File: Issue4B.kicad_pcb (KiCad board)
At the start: 2 copper layers, 213.1 x 130 mm, 207 parts, among them IC1 ULA, IC10 4116, IC11 4116, IC12 4116, IC13 4116, IC14 LM1889, IC15 4532, IC16 4532, IC17 4532, IC18 4532, IC19 4532, IC2 Z80, IC20 4532, IC21 4532, IC22 4532, IC23 LS32, IC24 LS00, IC25 LS157, IC26 LS157, IC3 LS157, IC4 LS157, IC5 ROM, IC6 4116, IC7 4116, IC8 4116, IC9 4116, J7 Barrel_Jack_MountingPin, SW1 SW_SPDT, T1 Transformer_1P_1S, X1 14Mhz, X2 4.43Mhz

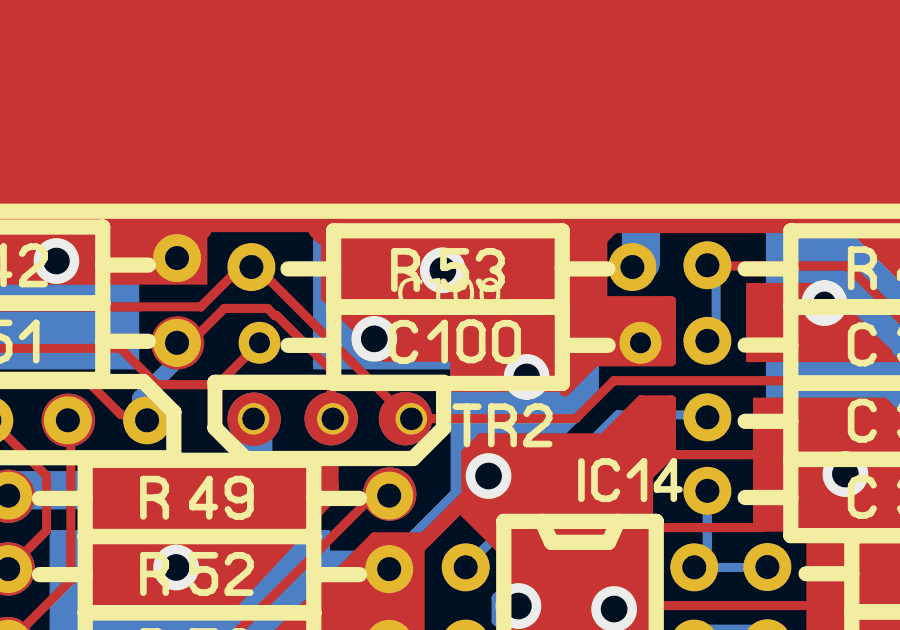
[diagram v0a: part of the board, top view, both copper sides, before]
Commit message: Correct values for C100 and C101
Update values and layout for C100 and C101. Taken from Issue 6A schematic.
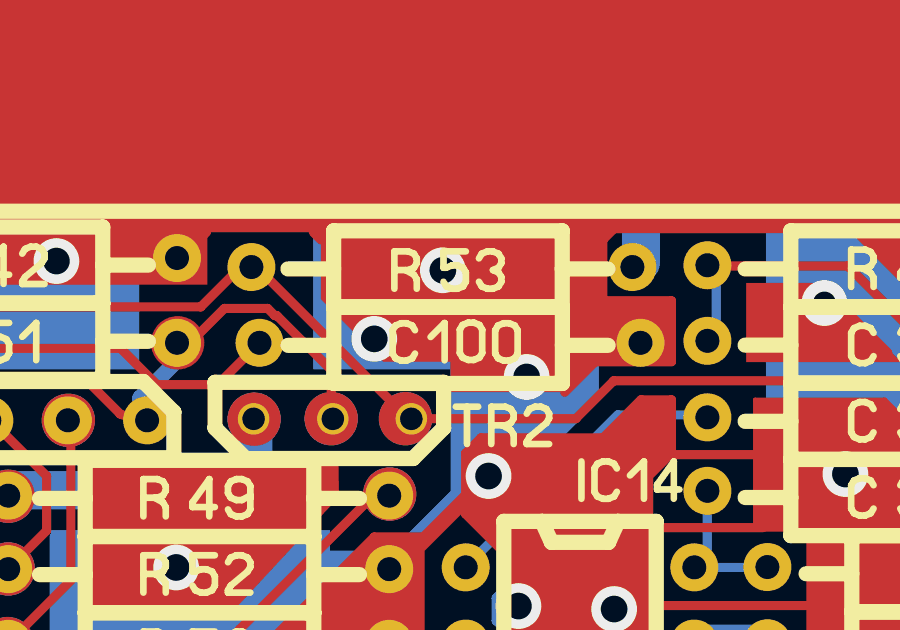
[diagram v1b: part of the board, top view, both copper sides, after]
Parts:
- C100: value 390R -> 10nF; footprint Mod:R_Yageo_L3.6mm_D1.6mm_P12.70mm_Horizontal -> Mod:C_Axial_L3.8mm_D2.6mm_P12.70mm_Horizontal
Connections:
- C101 pad 2: GND -> +V_IN
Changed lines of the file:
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@@
 		)
 	)
-	(footprint "Mod:R_Yageo_L3.6mm_D1.6mm_P12.70mm_Horizontal"
+	(footprint "Mod:C_Axial_L3.8mm_D2.6mm_P12.70mm_Horizontal"
 		(locked yes)
 		(layer "F.Cu")
 		(at 62.7695 63.526)
-		(descr "Resistor, Yageo series, Axial, Horizontal, pin pitch=12.7mm, 0.167W, length*diameter=3.6*1.6mm^2, http://cdn-reichelt.de/documents/datenblatt/B400/1_4W%23YAG.pdf")
-		(tags "Resistor Yageo series Axial Horizontal pin pitch 12.7mm 0.167W length 3.6mm diameter 1.6mm")
+		(descr "C, Axial series, Axial, Horizontal, pin pitch=12.7mm, length*diameter=3.8*2.6mm^2, http://www.vishay.com/docs/45231/arseries.pdf")
+		(tags "C Axial series Axial Horizontal pin pitch 12.7mm  length 3.8mm diameter 2.6mm")
 		(property "Reference" "C100"
-			(at 6.33 -1.62 0)
+			(at 6.35 0.127 0)
 			(layer "F.SilkS")
+			(hide yes)
 			(effects
 				(font
@@
 			)
 		)
-		(property "Value" "390R"
-			(at 6.35 -0.01 0)
+		(property "Value" "10nF"
+			(at 6.35 2.42 0)
 			(layer "F.Fab")
 			(effects
@@
 			)
 		)
-		(property "Description" ""
+		(property "Description" "Unpolarized capacitor, small symbol"
 			(at 0 0 0)
 			(layer "F.Fab")
@@
 			)
 		)
-		(property ki_fp_filters "R_*")
+		(property ki_fp_filters "C_*")
 		(sheetname "/")
 		(sheetfile "Issue4B.kicad_sch")
@@
 			)
 		)
-		(attr through_hole)
+		(attr through_hole dnp)
 		(duplicate_pad_numbers_are_jumpers no)
 		(fp_rect
-			(start -0.95 -1.05)
-			(end 13.65 1.05)
+			(start -1.05 -1.55)
+			(end 13.75 1.55)
 			(stroke
 				(width 0.05)
@@
 		)
 		(fp_line
-			(start 0 0)
-			(end 4.55 0)
+			(start 1.5 0)
+			(end 4.45 0)
 			(stroke
 				(width 0.1)
@@
 		)
 		(fp_line
-			(start 12.7 0)
-			(end 8.15 0)
+			(start 11.2 0)
+			(end 8.25 0)
 			(stroke
 				(width 0.1)
@@
 		)
 		(fp_rect
-			(start 4.55 -0.8)
-			(end 8.15 0.8)
+			(start 4.45 -1.2)
+			(end 8.25 1.2)
 			(stroke
 				(width 0.1)
@@
 			(effects
 				(font
-					(size 0.72 0.72)
-					(thickness 0.108)
+					(size 0.76 0.76)
+					(thickness 0.114)
 				)
 			)
@@
 		(pad "1" thru_hole circle
 			(at 0 0)
-			(size 1.4 1.4)
-			(drill 0.7)
+			(size 1.6 1.6)
+			(drill 0.8)
 			(layers "*.Cu" "*.Mask")
 			(remove_unused_layers no)
@@
 		(pad "2" thru_hole circle
 			(at 12.7 0)
-			(size 1.4 1.4)
-			(drill 0.7)
+			(size 1.6 1.6)
+			(drill 0.8)
 			(layers "*.Cu" "*.Mask")
 			(remove_unused_layers no)
@@
 		)
 		(embedded_fonts no)
-		(model "${KIPRJMOD}/STPS/Resistor-0207-6.3x2.4x12.70.STEP"
+		(model "${KIPRJMOD}/STPS/Capacitor Ceramic No Polarity axial 12.70.STEP"
 			(offset
-				(xyz 9.5 0 1.5)
+				(xyz 6.25 0 0)
 			)
 			(scale
@@
 			)
 			(rotate
-				(xyz -90 0 180)
+				(xyz -90 -0 -0)
 			)
 		)
@@
 			)
 		)
-		(attr through_hole)
+		(attr through_hole dnp)
 		(duplicate_pad_numbers_are_jumpers no)
 		(fp_line
@@
 			(layers "*.Cu" "*.Mask")
 			(remove_unused_layers no)
-			(net "GND")
+			(net "+V_IN")
 			(pintype "passive")
 		)
